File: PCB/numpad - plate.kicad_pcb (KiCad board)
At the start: 2 copper layers, 105.6 x 115.1 mm, 0 parts

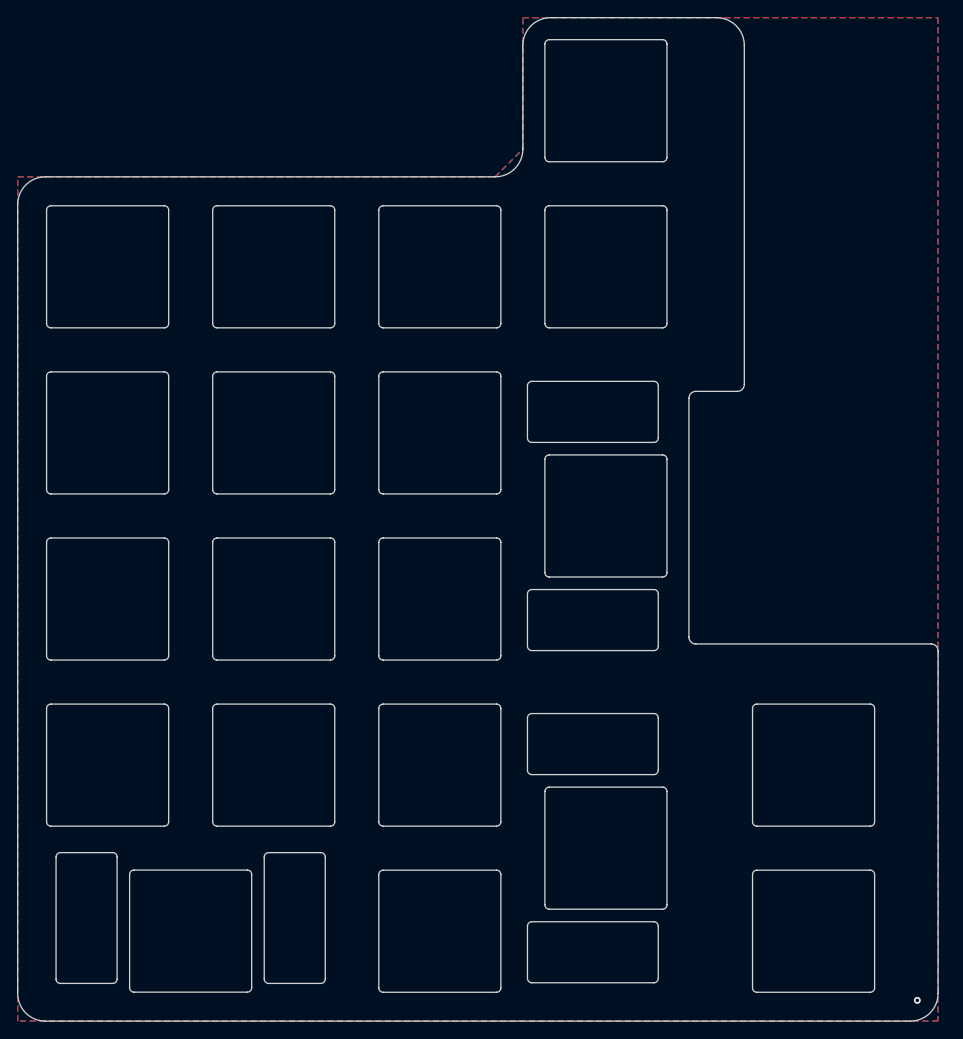
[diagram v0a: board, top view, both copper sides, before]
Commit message: Removed ground fill from plate
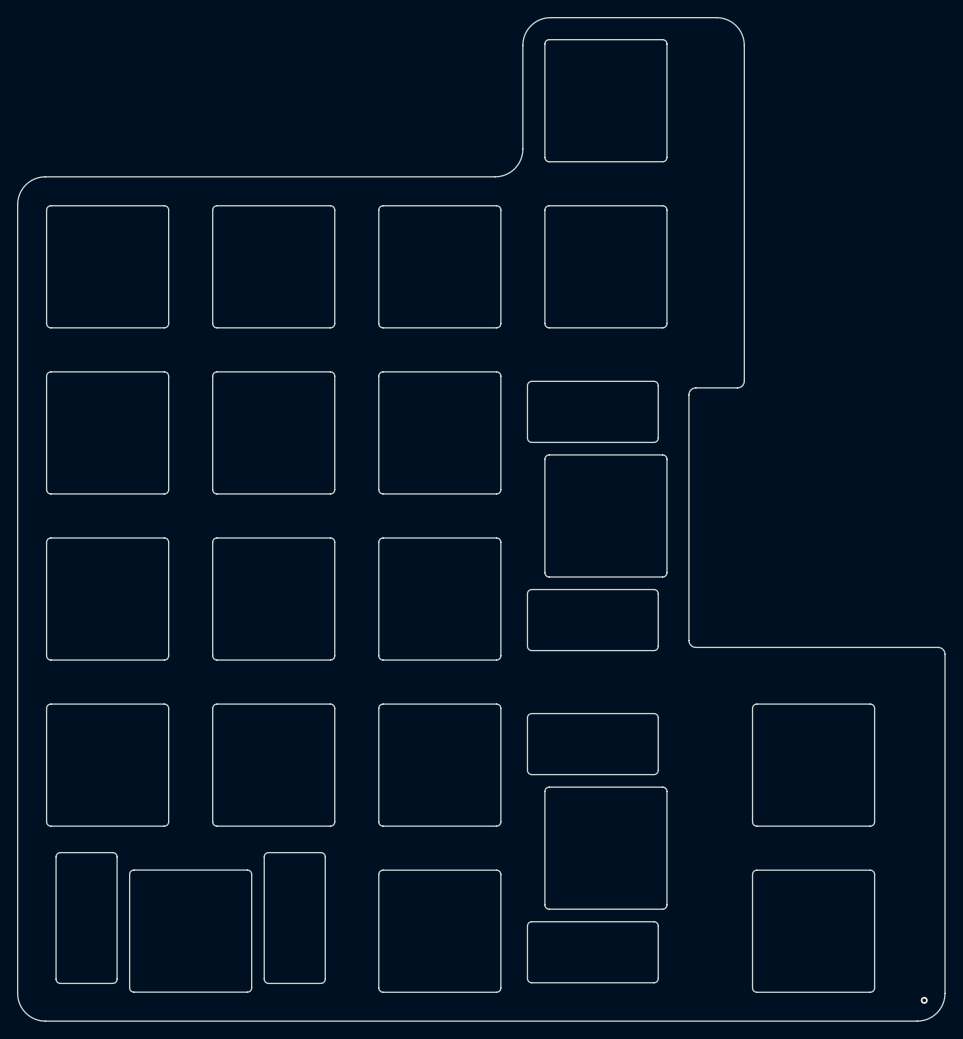
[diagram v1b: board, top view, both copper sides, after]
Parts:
- added logo: G***, custom_footprints:logo, F.Cu at (154.8, 139.7)
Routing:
- removed copper zone on B.Cu, net (none)
- removed copper zone on F.Cu, net (none)
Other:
- board size 105.6 x 115.1 mm -> 106.4 x 115.1 mm
- board text added: "JLCJLCJLCJLC"
- board text added: "howardt12345.com"
- board text added: "kb.ht12345.xyz/numpad"
- board text added: "numpad fr4 plate"
- board text added: "© 2022 Howard Tseng"

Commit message: changed plate url text
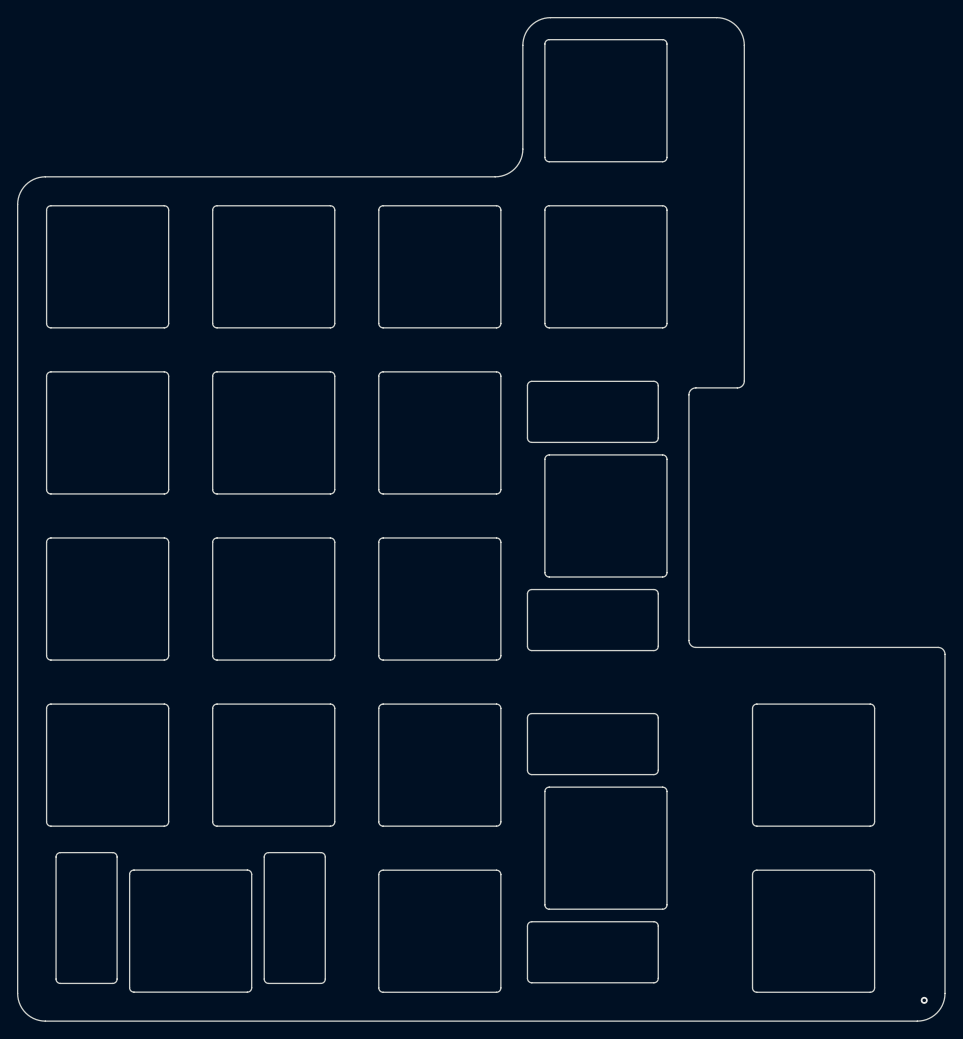
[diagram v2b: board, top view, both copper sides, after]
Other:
- net class Default removed
- board text added: "kb.ht12345.xyz/np0"
- board text removed: "kb.ht12345.xyz/numpad"
